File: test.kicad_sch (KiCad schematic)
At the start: 9 parts, among them U1 MSPM0G3507SPTR

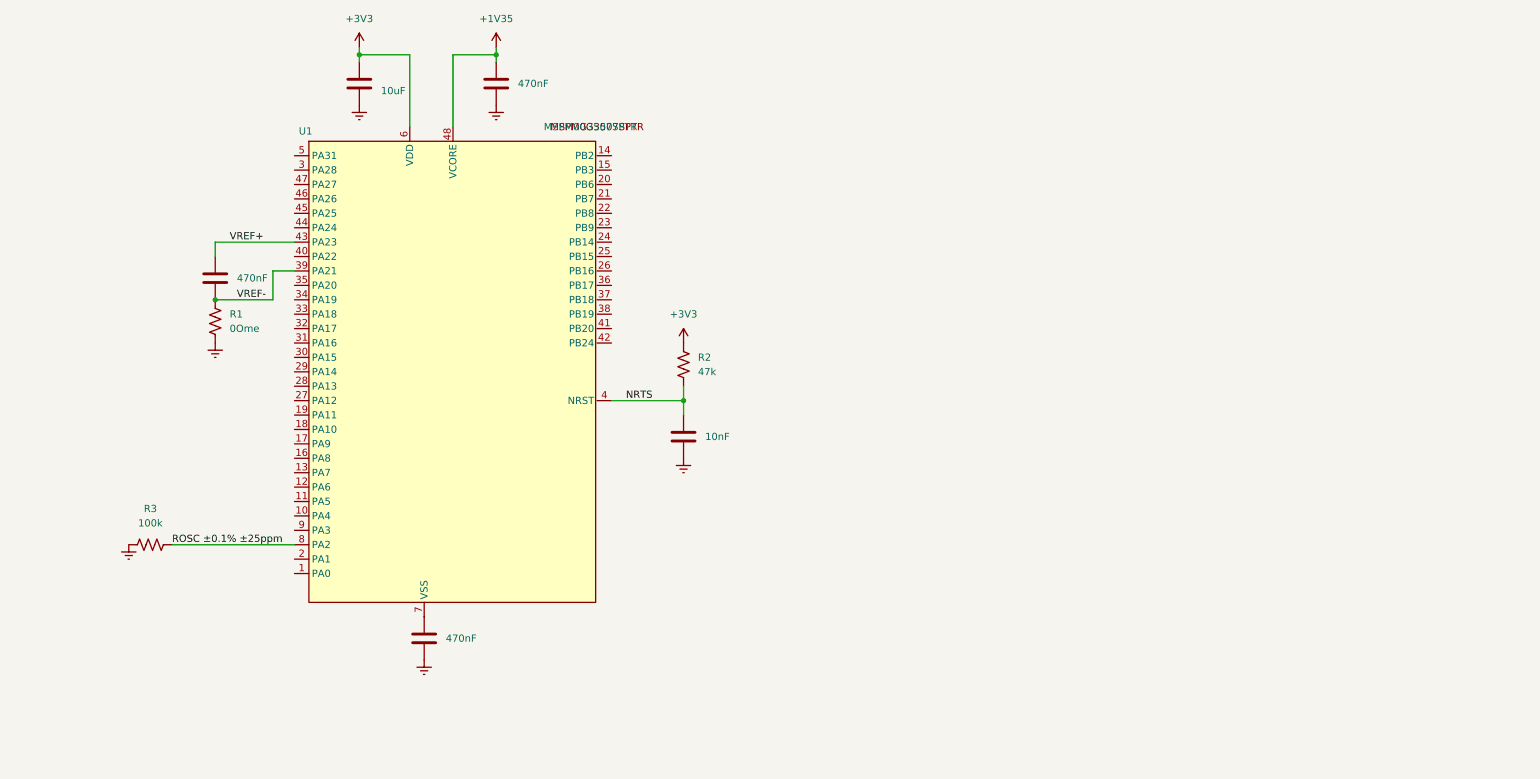
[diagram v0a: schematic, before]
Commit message: added an external 48MHz Crystal ,gonna take some time to study usb-c before adding it
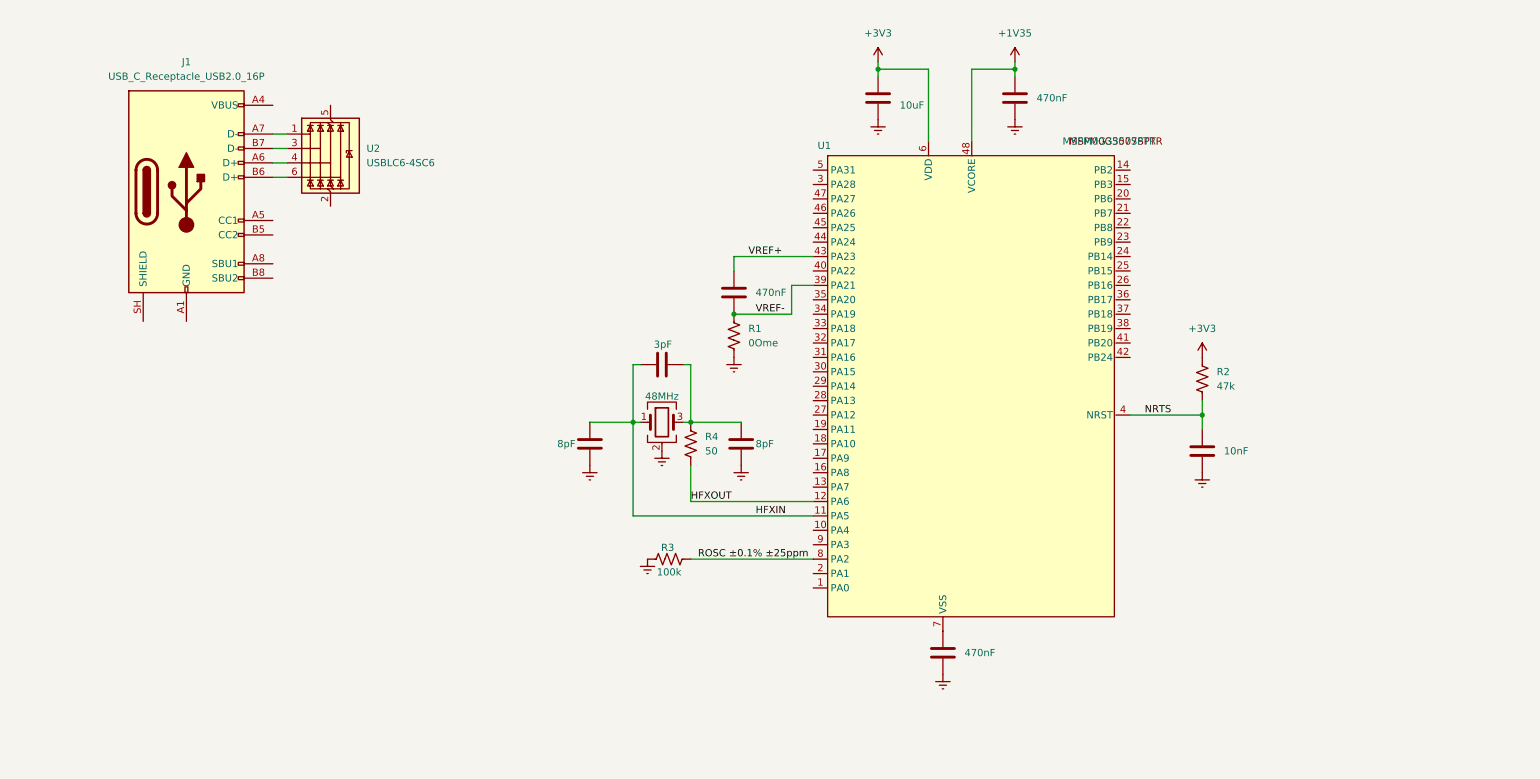
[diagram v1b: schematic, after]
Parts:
- added C7, C8: 8pF, Capacitor_SMD:C_0402_1005Metric_Pad0.74x0.62mm_HandSolder, symbol Device:C
- added C9: 3pF, Capacitor_SMD:C_0402_1005Metric_Pad0.74x0.62mm_HandSolder, symbol Device:C
- added J1: USB_C_Receptacle_USB2.0_16P, Package_DFN_QFN:WDFN-10-1EP_3x3mm_P0.5mm_EP1.8x2.5mm, symbol Connector:USB_C_Receptacle_USB2.0_16P
- added R4: 50, symbol Device:R_US
- added U2: USBLC6-4SC6, Package_TO_SOT_SMD:SOT-23-6, symbol Power_Protection:USBLC6-4SC6
- added Y1: 48MHz, Crystal:Crystal_SMD_2016-4Pin_2.0x1.6mm, symbol Device:Crystal_GND24
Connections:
- net Earth: now also C7.2, C8.2, Y1.2 (G), Y1.4 (G)
- net HFXIN: now reaches U1.11 (PA5)
- net HFXIN: now also C7.1, C9.1, Y1.1
- net HFXOUT: now reaches U1.12 (PA6)
- net HFXOUT: now also R4.1
- new net: C8.1, C9.2, R4.2, Y1.3
- new net: J1.A1 (GND), J1.A12 (GND), J1.B1 (GND), J1.B12 (GND)
- new net: J1.A4 (VBUS), J1.A9 (VBUS), J1.B4 (VBUS), J1.B9 (VBUS)
- new net: J1.A6 (D+), U2.4 (I/O3)
- new net: J1.A7 (D-), U2.1 (I/O1)
- new net: J1.B6 (D+), U2.6 (I/O4)
- new net: J1.B7 (D-), U2.3 (I/O2)
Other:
- moved on the sheet: R1, R2, R3, U1

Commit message: added a usb and usb to uart
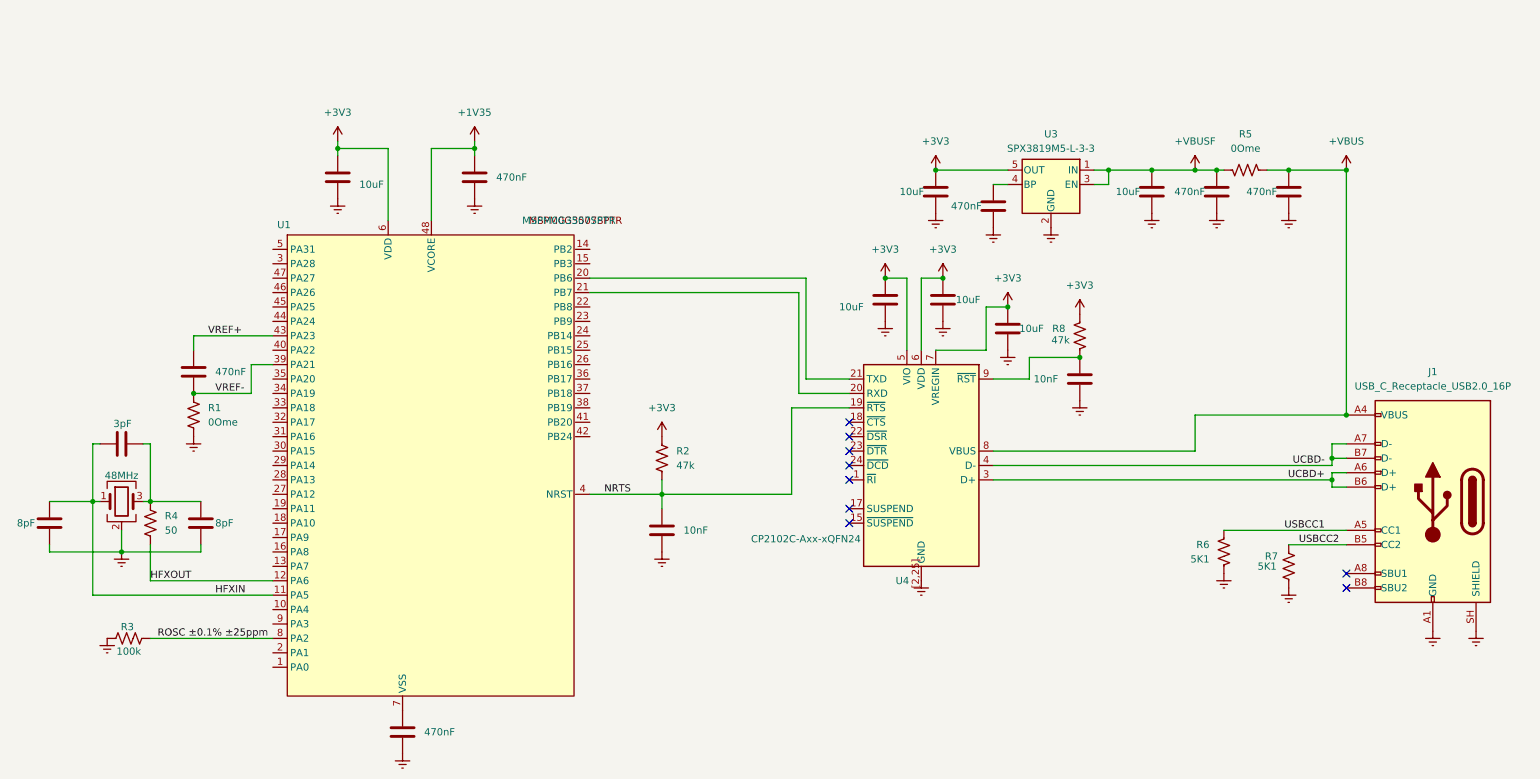
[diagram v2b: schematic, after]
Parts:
- removed U2: USBLC6-4SC6, Package_TO_SOT_SMD:SOT-23-6, symbol Power_Protection:USBLC6-4SC6
- added C10, C13, C6: 470nF, Package_QFP:LQFP-48_7x7mm_P0.5mm, symbol Device:C
- added C11, C12: 10uF, Package_QFP:LQFP-48_7x7mm_P0.5mm, symbol Device:C
- added C14, C16, C17: 10uF, Capacitor_SMD:C_0402_1005Metric_Pad0.74x0.62mm_HandSolder, symbol Device:C
- added C15: 10nF, Capacitor_SMD:C_0402_1005Metric_Pad0.74x0.62mm_HandSolder, symbol Device:C
- added R5: 0Ome, symbol Device:R_US
- added R6, R7: 5K1, symbol Device:R_US
- added R8: 47k, symbol Device:R_US
- added U3: SPX3819M5-L-3-3, Package_TO_SOT_SMD:SOT-23-5, symbol Regulator_Linear:SPX3819M5-L-3-3
- added U4: CP2102C-Axx-xQFN24, Package_DFN_QFN:WQFN-24-1EP_4x4mm_P0.5mm_EP2.45x2.45mm, symbol Interface_USB:CP2102C-Axx-xQFN24
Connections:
- net +3V3: now also C12.1, C14.1, C16.1, C17.1, R8.1, U3.5 (OUT), U4.5 (VIO), U4.6 (VDD), U4.7 (VREGIN)
- net Earth: now also J1.A1 (GND), J1.A12 (GND), J1.B1 (GND), J1.B12 (GND), J1.SH (SHIELD), C10.2, C11.2, C12.2, C13.2, C14.2, C15.2, C16.2, C17.2, C6.2, R6.1, R7.1, U3.2 (GND), U4.[2,25] (GND)
- net NRTS: now also U4.19 (~{RTS})
- net at U1.20 (PB6): now also U4.21 (TXD)
- net at U1.21 (PB7): now also U4.20 (RXD)
- net +VBUS: now reaches J1.A4 (VBUS), J1.A9 (VBUS), J1.B4 (VBUS), J1.B9 (VBUS)
- net +VBUS: now also C6.1, R5.1, U4.8 (VBUS)
- net USBCC1: now reaches J1.A5 (CC1)
- net USBCC1: now also R6.2
- net UCBD+: now reaches J1.A6 (D+)
- net UCBD+: now also J1.B6 (D+), U4.3 (D+)
- net UCBD-: now reaches J1.A7 (D-)
- net UCBD-: now also J1.B7 (D-), U4.4 (D-)
- net USBCC2: now reaches J1.B5 (CC2)
- net USBCC2: now also R7.2
- new net: C13.1, U3.4 (BP)
- new net: C15.1, R8.2, U4.9 (~{RST})
- new net +VBUSF: C10.1, C11.1, R5.2, U3.1 (IN), U3.3 (EN)
- no-connect marks 0 -> 9
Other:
- moved on the sheet: J1, R1, R2, R3, R4, U1
